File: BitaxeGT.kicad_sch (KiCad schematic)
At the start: 1 part, among them J1 XT30

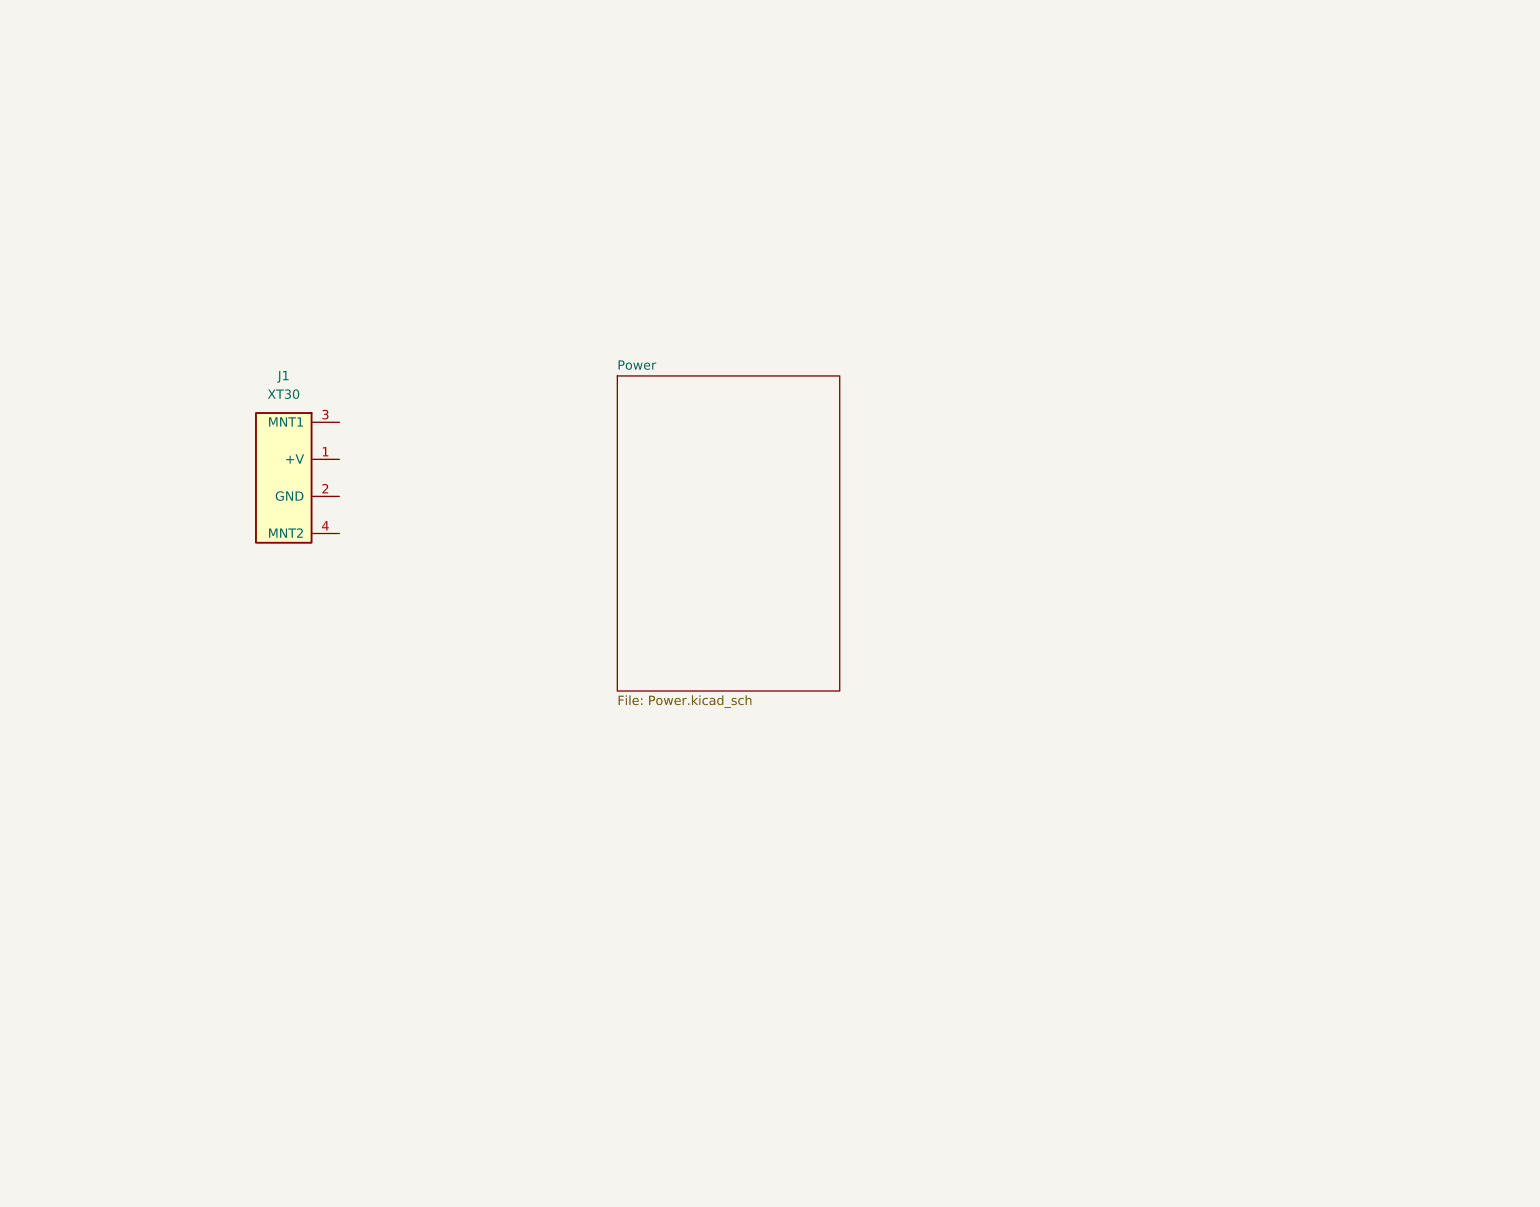
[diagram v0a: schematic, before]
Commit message: Add sheets and work on power supply
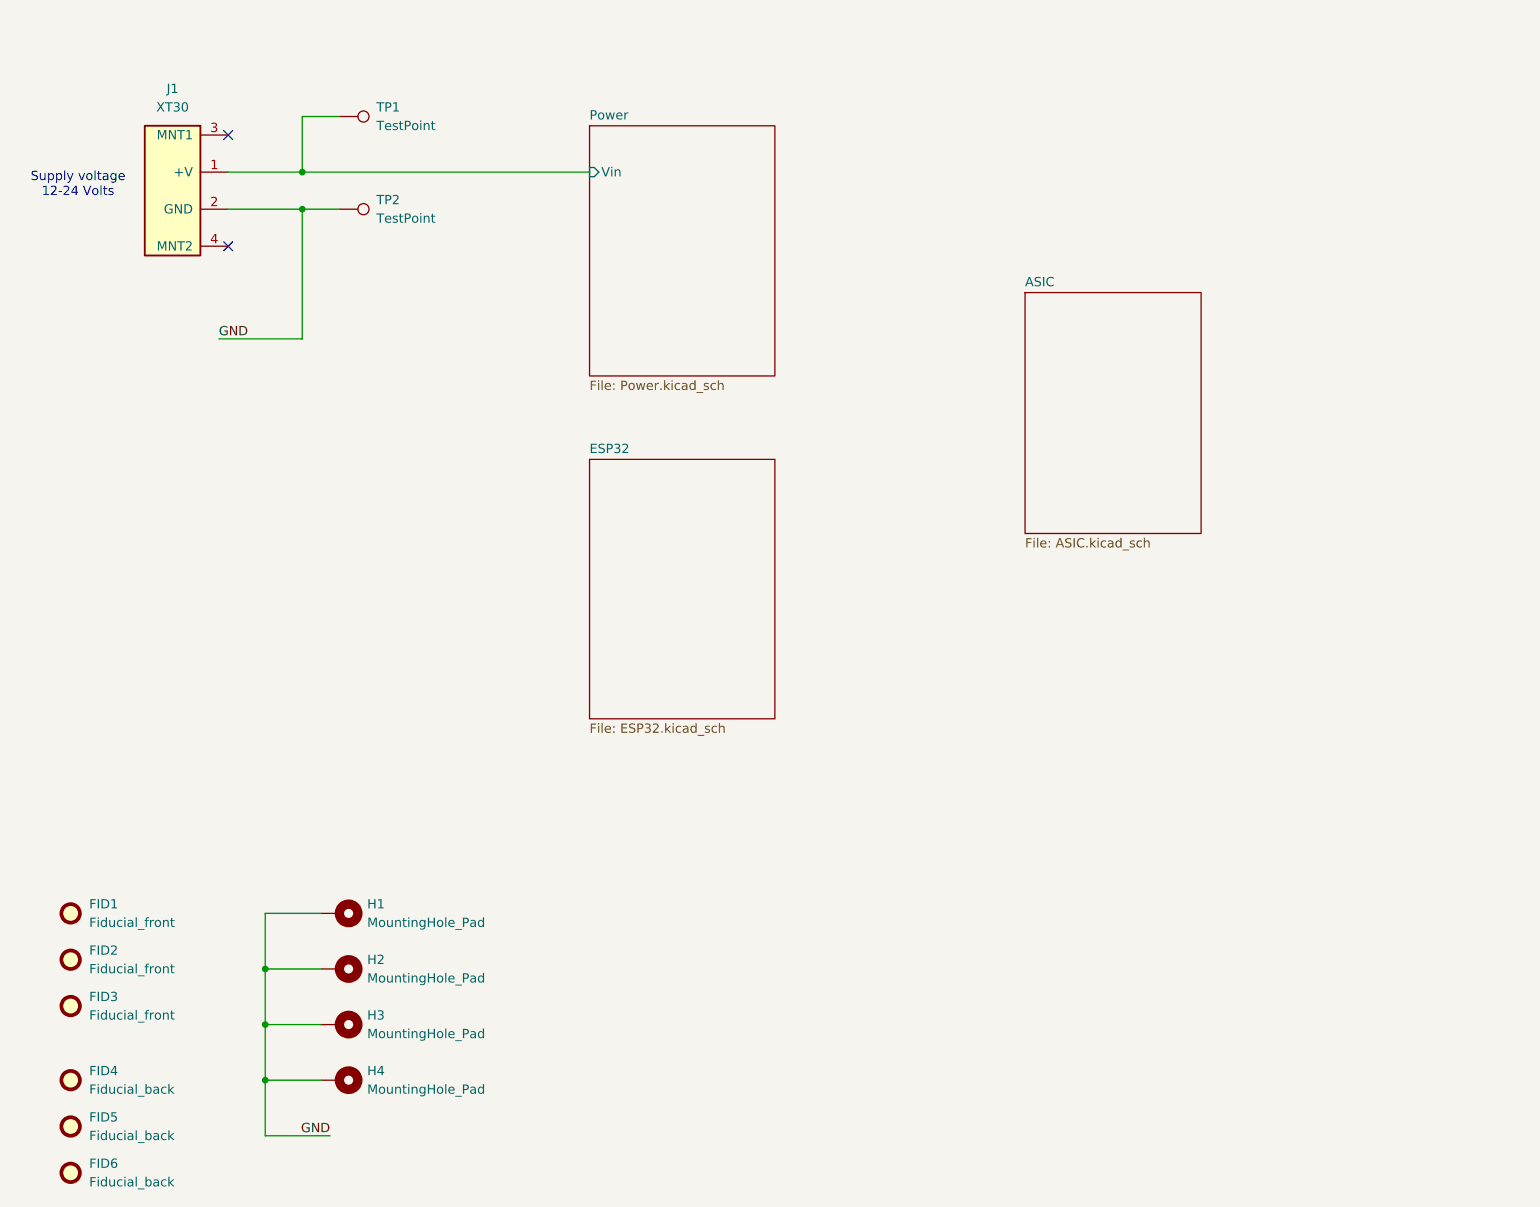
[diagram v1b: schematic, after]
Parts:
- added FID1, FID2, FID3: Fiducial_front, Fiducial:Fiducial_1mm_Mask2mm, symbol Mechanical:Fiducial
- added FID4, FID5, FID6: Fiducial_back, Fiducial:Fiducial_1mm_Mask2mm, symbol Mechanical:Fiducial
- added H1, H2, H3, H4: MountingHole_Pad, MountingHole:MountingHole_3.2mm_M3_Pad_Via, symbol Mechanical:MountingHole_Pad
- added TP1, TP2: TestPoint, symbol Connector:TestPoint
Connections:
- net Power/Vin: now reaches J1.1 (+V)
- net Power/Vin: now also TP1.1
- net GND: now reaches J1.2 (GND)
- net GND: now also H1.1, H2.1, H3.1, H4.1, TP2.1
- no-connect marks 0 -> 2
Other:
- added sheet ASIC (ASIC.kicad_sch)
- added sheet ESP32 (ESP32.kicad_sch)
- sheet Power ports: added Vin; removed none
- note added: "Supply voltage 12-24 Volts"
- moved on the sheet: J1

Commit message: More schematic work for ASICs and ESP32
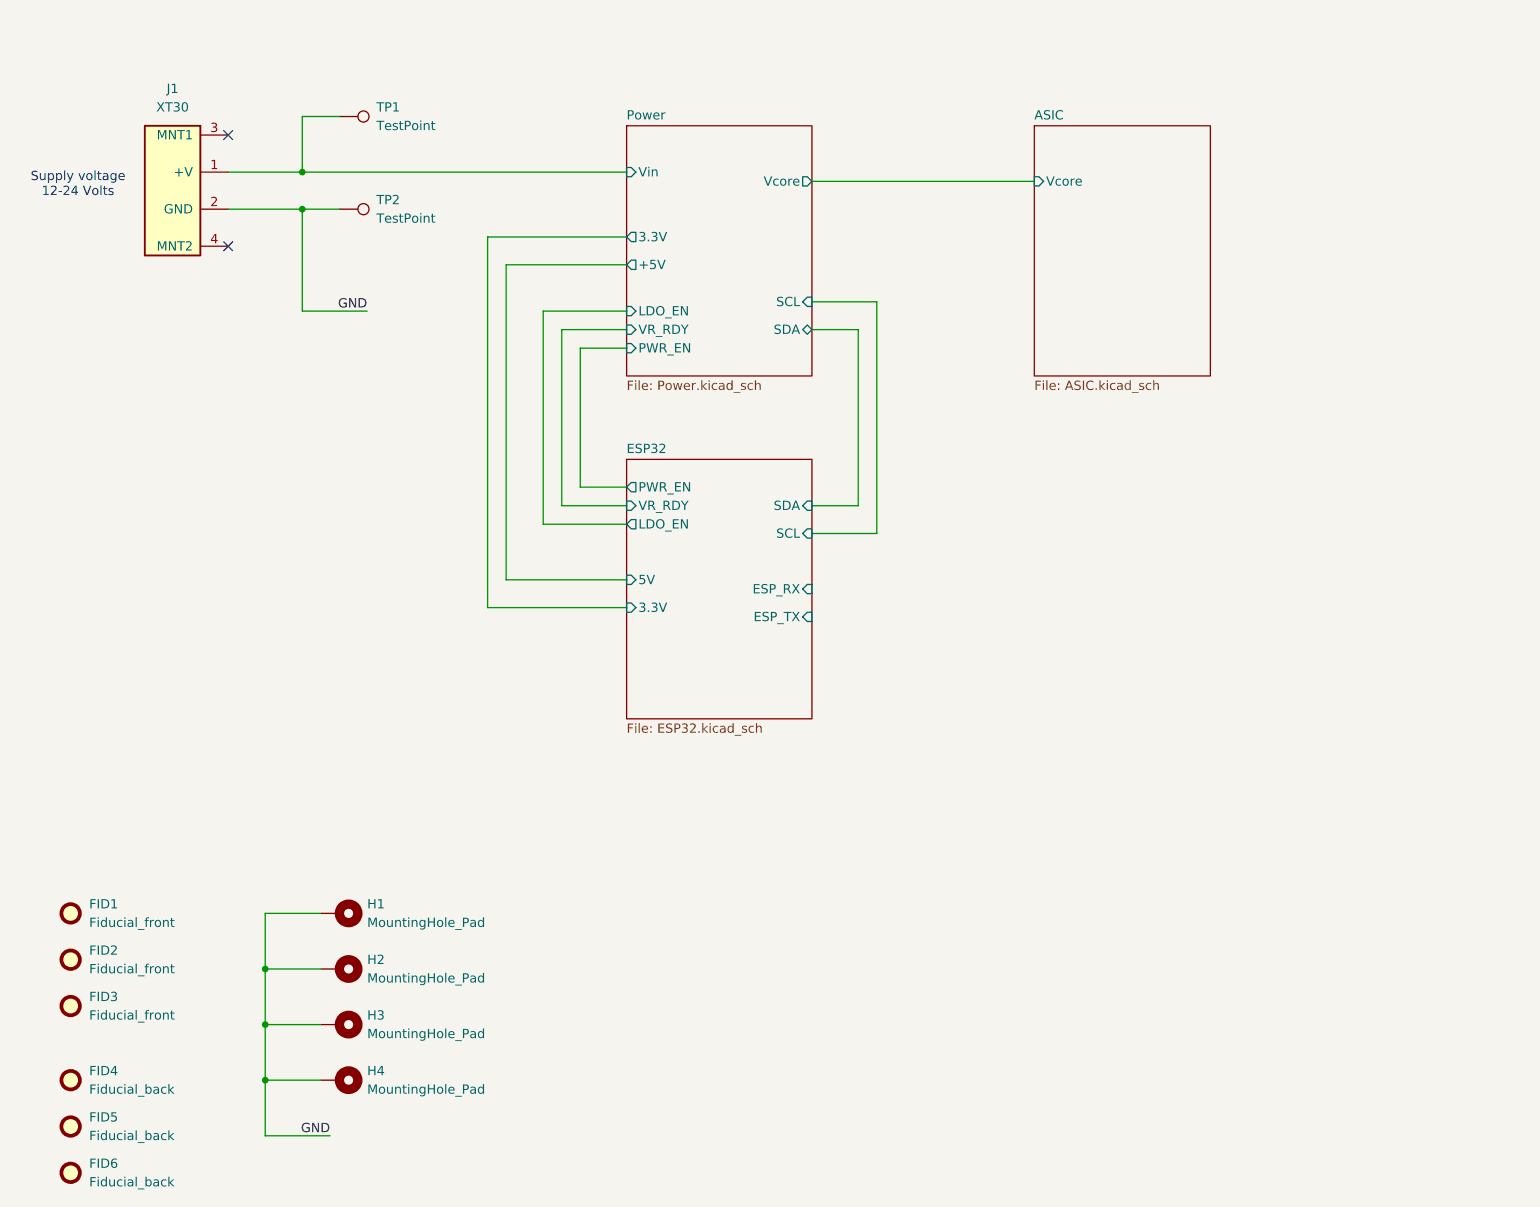
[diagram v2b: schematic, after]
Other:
- sheet ASIC ports: added Vcore; removed none
- sheet ESP32 ports: added 3.3V, 5V, ESP_RX, ESP_TX, LDO_EN, PWR_EN, SCL, SDA, VR_RDY; removed none
- sheet Power ports: added +5V, 3.3V, LDO_EN, PWR_EN, SCL, SDA, VR_RDY, Vcore; removed none

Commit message: add current sensor
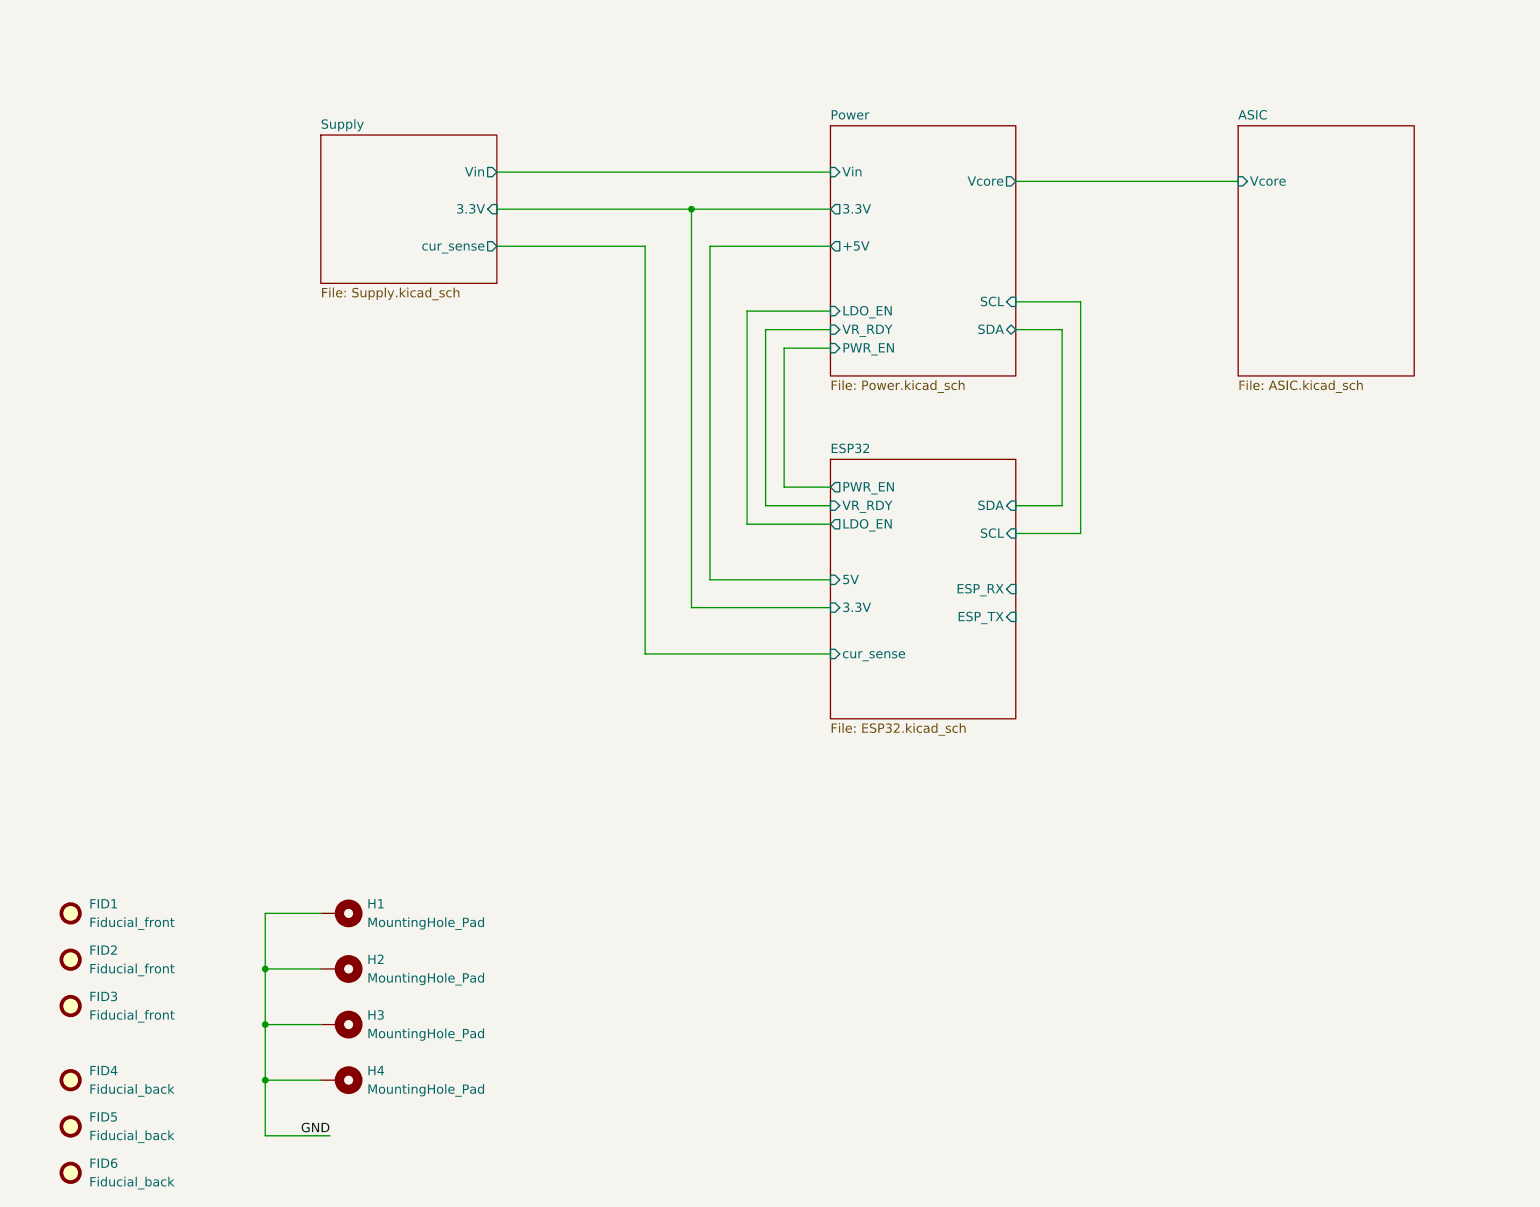
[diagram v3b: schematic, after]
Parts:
- removed J1: XT30, bitaxe:XT30PW-M, symbol bitaxe:XT30PW-M
- removed TP1, TP2: TestPoint, symbol Connector:TestPoint
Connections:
- no-connect marks 2 -> 0
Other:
- added sheet Supply (Supply.kicad_sch)
- sheet ESP32 ports: added cur_sense; removed none
- note removed: "Supply voltage 12-24 Volts"

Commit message: Finish wiring ASICs and ESP32
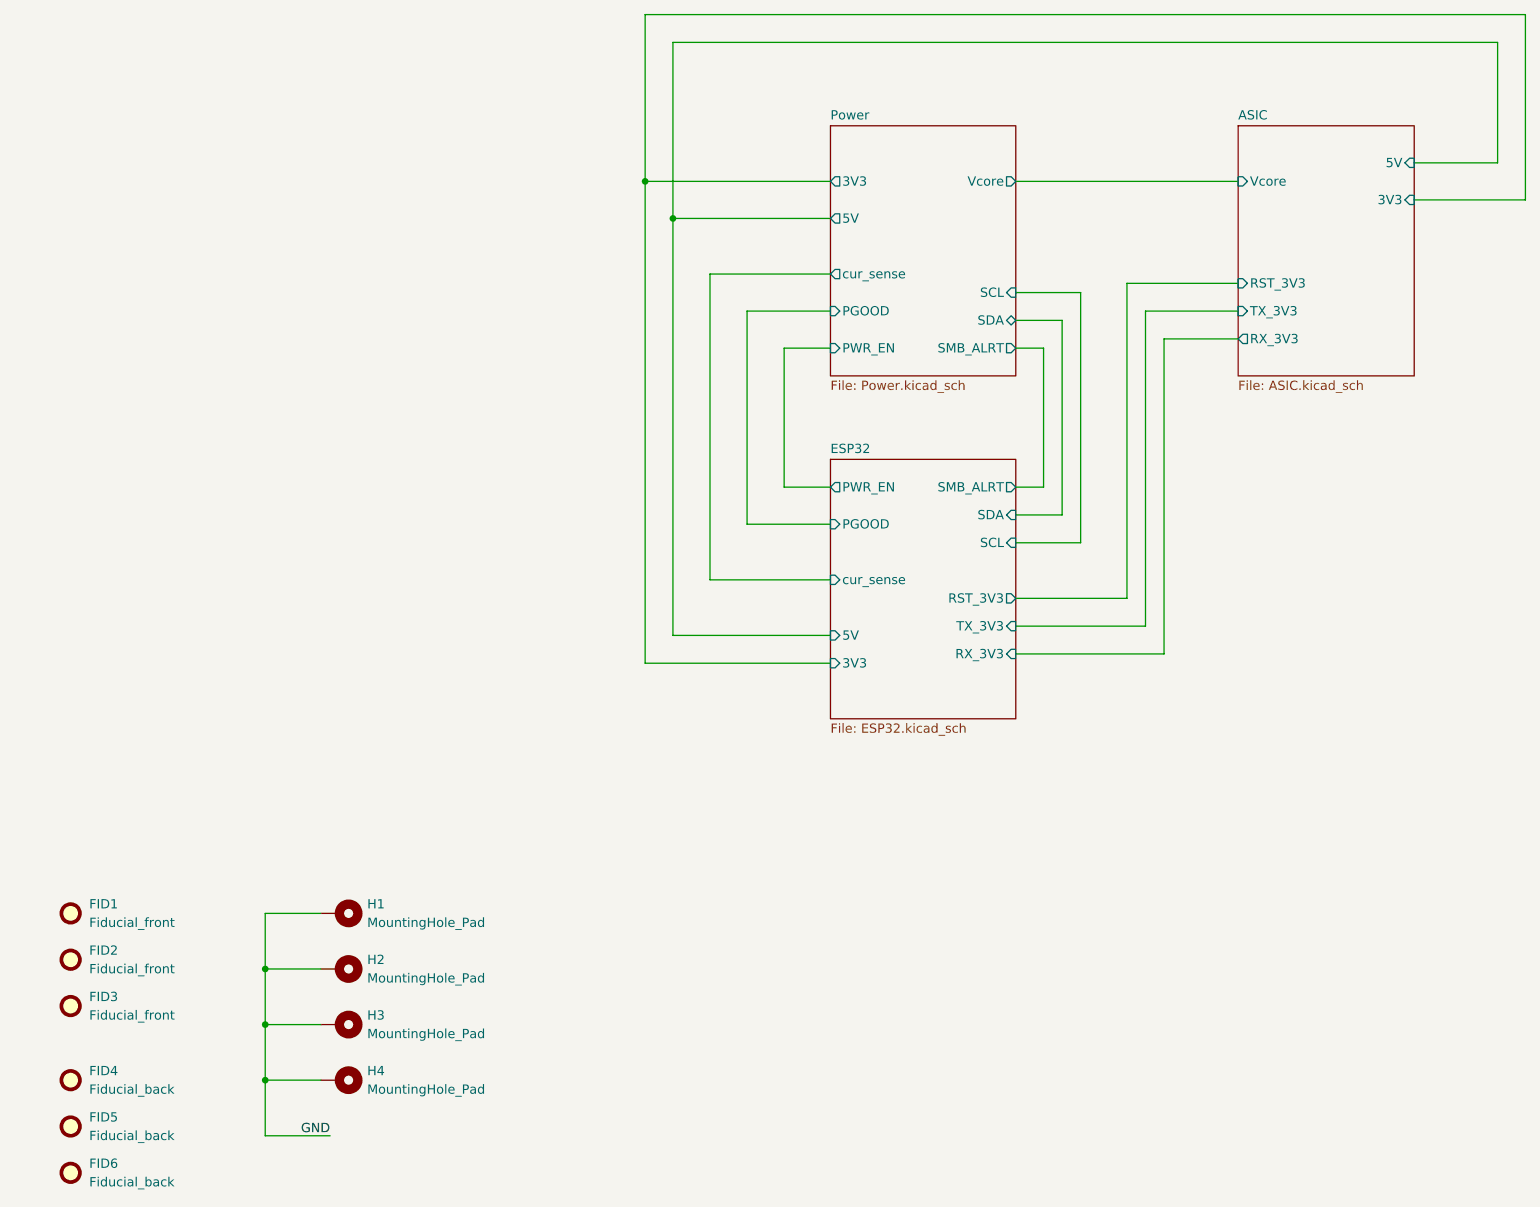
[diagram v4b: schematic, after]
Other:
- removed sheet Supply
- sheet ASIC ports: added 3V3, 5V, RST_3V3, RX_3V3, TX_3V3; removed none
- sheet ESP32 ports: added 3V3, PGOOD, RST_3V3, RX_3V3, SMB_ALRT, TX_3V3; removed 3.3V, ESP_RX, ESP_TX, LDO_EN, VR_RDY
- sheet Power ports: added 3V3, 5V, PGOOD, SMB_ALRT, cur_sense; removed +5V, 3.3V, LDO_EN, VR_RDY, Vin
